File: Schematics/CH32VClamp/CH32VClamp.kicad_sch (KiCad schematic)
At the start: 27 parts, among them J1 USB_C_Receptacle_USB2.0, J2 PGM, J3 OPGM, Q1 SE4625-PandN, Q2 SE4625-PandN, SW2 SW_MEC_5E, U1 ESP32-S2, U2 AP1117-33, Y1 40MHz

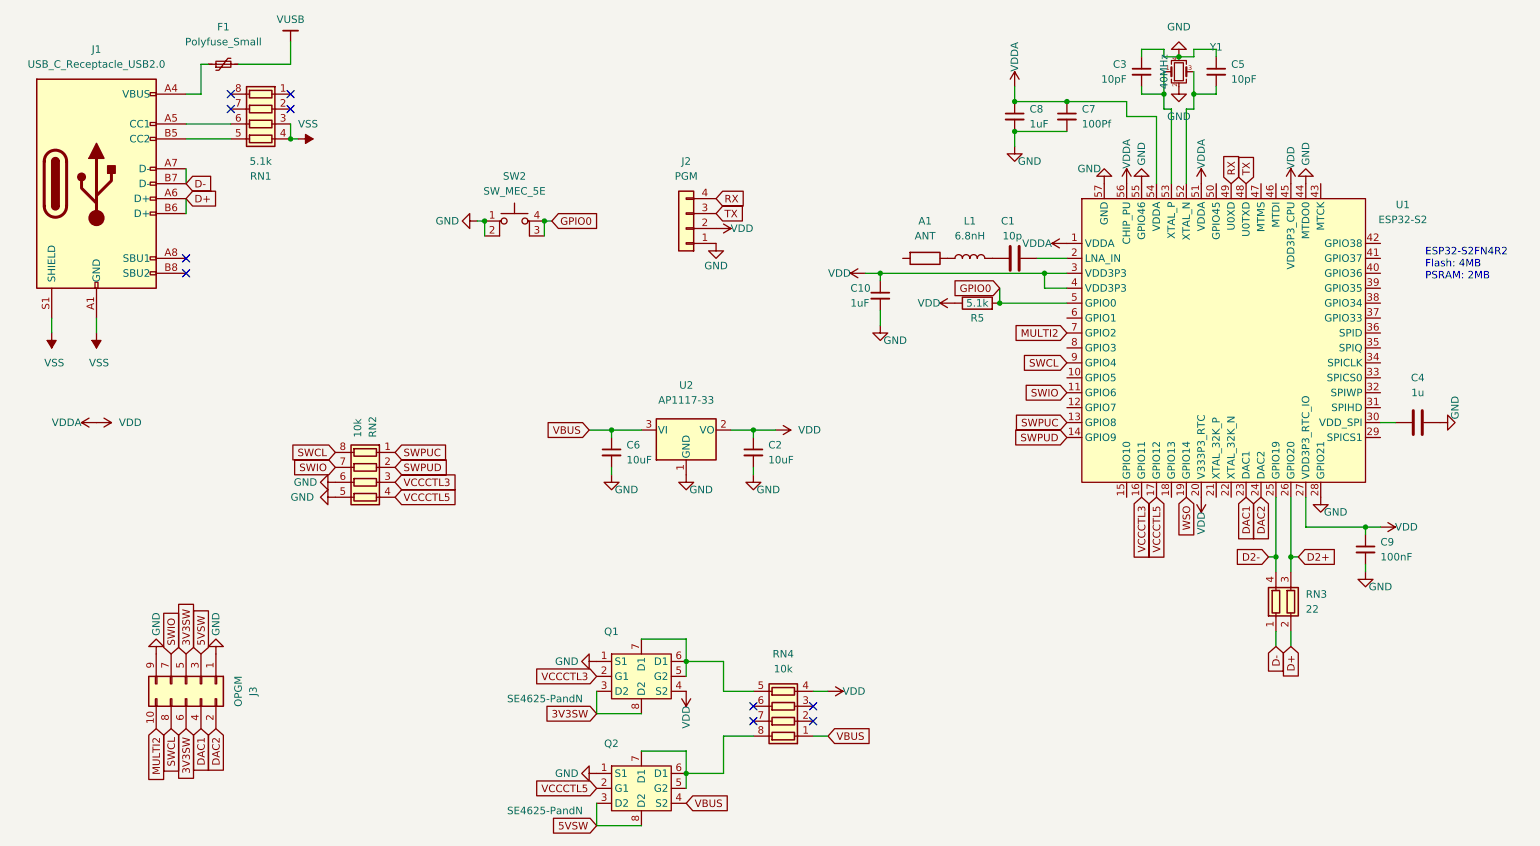
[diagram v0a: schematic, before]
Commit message: Decide on standard and started routing
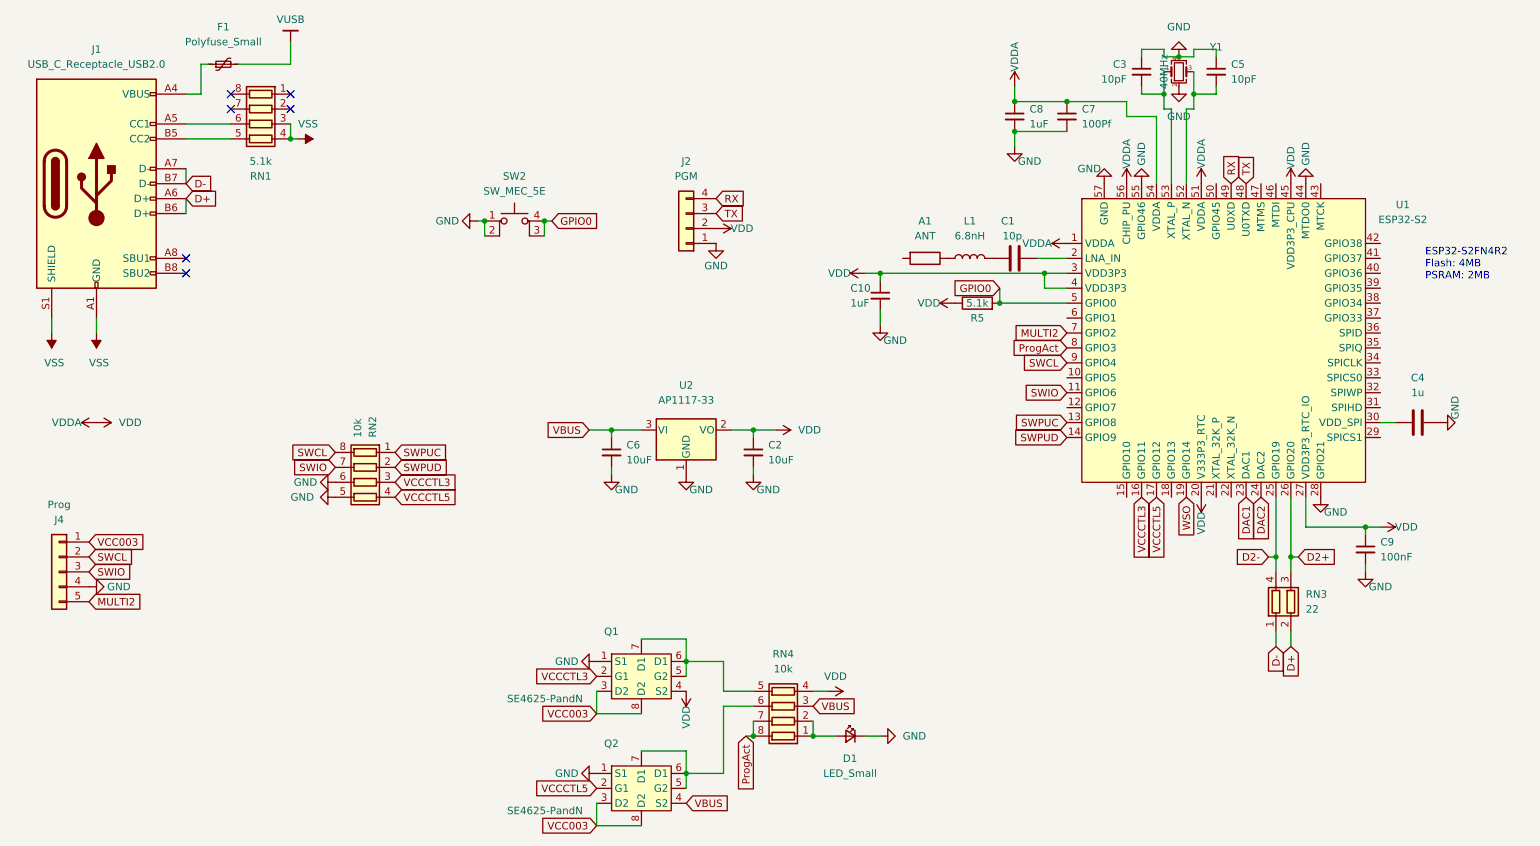
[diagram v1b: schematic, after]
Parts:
- removed J3: OPGM, Connector_PinHeader_2.54mm:PinHeader_2x05_P2.54mm_Horizontal, symbol Connector_Generic:Conn_02x05_Odd_Even
- added D1: LED_Small, LED_SMD:LED_0603_1608Metric, symbol Device:LED_Small
- added J4: Prog, Connector_PinHeader_2.54mm:PinHeader_1x05_P2.54mm_Vertical, symbol Connector_Generic:Conn_01x05
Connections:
- net 5VSW is gone; now on net VCC003: Q2.3 (D2), Q2.8 (D2)
- net GND: now also D1.1 (K), J4.4 (Pin_4)
- net MULTI2: now also J4.5 (Pin_5)
- net SWCL: now also J4.2 (Pin_2)
- net SWIO: now also J4.3 (Pin_3)
- net VBUS: now also RN4.3 (R3.1); no longer RN4.1 (R1.1)
- net ProgAct: now reaches U1.8 (GPIO3)
- net ProgAct: now also RN4.7 (R2.2), RN4.8 (R1.2)
- net at RN4.2 (R2.1): now also RN4.1 (R1.1), D1.2 (A)
- net at RN4.6 (R3.2): now also Q2.5 (G2), Q2.6 (D1), Q2.7 (D1)
- net 3V3SW renamed VCC003
- net VCC003: now also J4.1 (Pin_1)
- no-connect marks 10 -> 6

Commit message: Ordered CH32V Clamp V1
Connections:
- net VSS is gone; now on net GND: J1.A1 (GND), J1.A12 (GND), J1.B1 (GND), J1.B12 (GND), J1.S1 (SHIELD), RN1.3 (R3.1), RN1.4 (R4.1)
- net VUSB is gone; now on net VBUS: F1.2
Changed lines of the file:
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@@
-    (stroke (width 0) (type default))
-  )
-  (wire (pts (xy 66.04 25.4) (xy 66.04 21.59))
     (stroke (width 0) (type default))
   )
@@
     )
   )
+  (global_label "VBUS" (shape input) (at 66.04 25.4 0) (fields_autoplaced)
+    (effects (font (size 1.27 1.27)) (justify left))
+    (property "Intersheetrefs" "${INTERSHEET_REFS}" (at 73.3517 25.4794 0)
+      (effects (font (size 1.27 1.27)) (justify left) hide)
+    )
+  )
   (global_label "VBUS" (shape input) (at 154.94 134.62 0) (fields_autoplaced)
     (effects (font (size 1.27 1.27)) (justify left))
@@
     )
   )
+  (symbol (lib_id "power:GND") (at 33.02 71.12 0) (unit 1)
+    (in_bom yes) (on_board yes) (dnp no)
+    (property "Reference" "#PWR02" (at 33.02 77.47 0)
+      (effects (font (size 1.27 1.27)) hide)
+    )
+    (property "Value" "GND" (at 33.02 76.2 90)
+      (effects (font (size 1.27 1.27)))
+    )
+    (property "Footprint" "" (at 33.02 71.12 0)
+      (effects (font (size 1.27 1.27)) hide)
+    )
+    (property "Datasheet" "" (at 33.02 71.12 0)
+      (effects (font (size 1.27 1.27)) hide)
+    )
+    (pin "1")
+    (instances
+      (project "CH32VClamp"
+        (path "/3c272da4-3810-4d6a-a6aa-4e1cad4b6a87"
+          (reference "#PWR02") (unit 1)
+        )
+      )
+      (project "esp32s2-funprog"
+        (path "/e63e39d7-6ac0-4ffd-8aa3-1841a4541b55"
+          (reference "#PWR0108") (unit 1)
+        )
+      )
+    )
+  )
   (symbol (lib_id "power:VDD") (at 138.43 53.34 270) (unit 1)
     (in_bom yes) (on_board yes) (dnp no)
@@
         (path "/e63e39d7-6ac0-4ffd-8aa3-1841a4541b55"
           (reference "#PWR0119") (unit 1)
+        )
+      )
+    )
+  )
+  (symbol (lib_id "power:GND") (at 25.4 71.12 0) (unit 1)
+    (in_bom yes) (on_board yes) (dnp no)
+    (property "Reference" "#PWR01" (at 25.4 77.47 0)
+      (effects (font (size 1.27 1.27)) hide)
+    )
+    (property "Value" "GND" (at 25.4 76.2 90)
+      (effects (font (size 1.27 1.27)))
+    )
+    (property "Footprint" "" (at 25.4 71.12 0)
+      (effects (font (size 1.27 1.27)) hide)
+    )
+    (property "Datasheet" "" (at 25.4 71.12 0)
+      (effects (font (size 1.27 1.27)) hide)
+    )
+    (pin "1")
+    (instances
+      (project "CH32VClamp"
+        (path "/3c272da4-3810-4d6a-a6aa-4e1cad4b6a87"
+          (reference "#PWR01") (unit 1)
+        )
+      )
+      (project "esp32s2-funprog"
+        (path "/e63e39d7-6ac0-4ffd-8aa3-1841a4541b55"
+          (reference "#PWR0108") (unit 1)
         )
       )
@@
         (path "/e63e39d7-6ac0-4ffd-8aa3-1841a4541b55"
           (reference "#PWR0117") (unit 1)
-        )
-      )
-    )
-  )
-  (symbol (lib_id "power:VSS") (at 33.02 71.12 180) (unit 1)
-    (in_bom yes) (on_board yes) (dnp no)
-    (property "Reference" "#PWR02" (at 33.02 67.31 0)
-      (effects (font (size 1.27 1.27)) hide)
-    )
-    (property "Value" "VSS" (at 31.75 76.2 0)
-      (effects (font (size 1.27 1.27)) (justify right))
-    )
-    (property "Footprint" "" (at 33.02 71.12 0)
-      (effects (font (size 1.27 1.27)) hide)
-    )
-    (property "Datasheet" "" (at 33.02 71.12 0)
-      (effects (font (size 1.27 1.27)) hide)
-    )
-    (pin "1")
-    (instances
-      (project "CH32VClamp"
-        (path "/3c272da4-3810-4d6a-a6aa-4e1cad4b6a87"
-          (reference "#PWR02") (unit 1)
-        )
-      )
-      (project "ReflowReview"
-        (path "/91523ecc-b630-476b-a03e-91f84cd87a20"
-          (reference "#PWR021") (unit 1)
-        )
-      )
-      (project "SerialClamp"
-        (path "/ad13f272-13a7-4209-a78a-add31e33c82c"
-          (reference "#PWR03") (unit 1)
-        )
-      )
-      (project "AccelAssemblyTester"
-        (path "/b10930b8-2990-46a8-9d87-f0faa73d38e1"
-          (reference "#PWR018") (unit 1)
         )
       )
@@
     )
   )
-  (symbol (lib_id "power:VSS") (at 25.4 71.12 180) (unit 1)
-    (in_bom yes) (on_board yes) (dnp no)
-    (property "Reference" "#PWR01" (at 25.4 67.31 0)
-      (effects (font (size 1.27 1.27)) hide)
-    )
-    (property "Value" "VSS" (at 24.13 76.2 0)
-      (effects (font (size 1.27 1.27)) (justify right))
-    )
-    (property "Footprint" "" (at 25.4 71.12 0)
-      (effects (font (size 1.27 1.27)) hide)
-    )
-    (property "Datasheet" "" (at 25.4 71.12 0)
-      (effects (font (size 1.27 1.27)) hide)
-    )
-    (pin "1")
-    (instances
-      (project "CH32VClamp"
-        (path "/3c272da4-3810-4d6a-a6aa-4e1cad4b6a87"
-          (reference "#PWR01") (unit 1)
-        )
-      )
-      (project "ReflowReview"
-        (path "/91523ecc-b630-476b-a03e-91f84cd87a20"
-          (reference "#PWR01") (unit 1)
-        )
-      )
-      (project "SerialClamp"
-        (path "/ad13f272-13a7-4209-a78a-add31e33c82c"
-          (reference "#PWR02") (unit 1)
-        )
-      )
-      (project "AccelAssemblyTester"
-        (path "/b10930b8-2990-46a8-9d87-f0faa73d38e1"
-          (reference "#PWR018") (unit 1)
+  (symbol (lib_id "power:GND") (at 67.31 38.1 90) (unit 1)
+    (in_bom yes) (on_board yes) (dnp no)
+    (property "Reference" "#PWR04" (at 73.66 38.1 0)
+      (effects (font (size 1.27 1.27)) hide)
+    )
+    (property "Value" "GND" (at 72.39 38.1 90)
+      (effects (font (size 1.27 1.27)))
+    )
+    (property "Footprint" "" (at 67.31 38.1 0)
+      (effects (font (size 1.27 1.27)) hide)
+    )
+    (property "Datasheet" "" (at 67.31 38.1 0)
+      (effects (font (size 1.27 1.27)) hide)
+    )
+    (pin "1")
+    (instances
+      (project "CH32VClamp"
+        (path "/3c272da4-3810-4d6a-a6aa-4e1cad4b6a87"
+          (reference "#PWR04") (unit 1)
+        )
+      )
+      (project "esp32s2-funprog"
+        (path "/e63e39d7-6ac0-4ffd-8aa3-1841a4541b55"
+          (reference "#PWR0108") (unit 1)
         )
       )
@@
         (path "/3c272da4-3810-4d6a-a6aa-4e1cad4b6a87"
           (reference "C3") (unit 1)
-        )
-      )
-    )
-  )
-  (symbol (lib_id "power:VSS") (at 67.31 38.1 270) (unit 1)
-    (in_bom yes) (on_board yes) (dnp no)
-    (property "Reference" "#PWR04" (at 63.5 38.1 0)
-      (effects (font (size 1.27 1.27)) hide)
-    )
-    (property "Value" "VSS" (at 67.31 35.56 90)
-      (effects (font (size 1.27 1.27)) (justify left))
-    )
-    (property "Footprint" "" (at 67.31 38.1 0)
-      (effects (font (size 1.27 1.27)) hide)
-    )
-    (property "Datasheet" "" (at 67.31 38.1 0)
-      (effects (font (size 1.27 1.27)) hide)
-    )
-    (pin "1")
-    (instances
-      (project "CH32VClamp"
-        (path "/3c272da4-3810-4d6a-a6aa-4e1cad4b6a87"
-          (reference "#PWR04") (unit 1)
-        )
-      )
-      (project "ReflowReview"
-        (path "/91523ecc-b630-476b-a03e-91f84cd87a20"
-          (reference "#PWR02") (unit 1)
-        )
-      )
-      (project "SerialClamp"
-        (path "/ad13f272-13a7-4209-a78a-add31e33c82c"
-          (reference "#PWR05") (unit 1)
-        )
-      )
-      (project "AccelAssemblyTester"
-        (path "/b10930b8-2990-46a8-9d87-f0faa73d38e1"
-          (reference "#PWR036") (unit 1)
         )
       )
@@
     )
   )
-  (symbol (lib_id "gkl_power:VUSB") (at 66.04 21.59 0) (unit 1)
-    (in_bom yes) (on_board yes) (dnp no) (fields_autoplaced)
-    (property "Reference" "#PWR03" (at 66.04 25.4 0)
-      (effects (font (size 1.27 1.27)) hide)
-    )
-    (property "Value" "VUSB" (at 66.04 17.78 0)
-      (effects (font (size 1.27 1.27)))
-    )
-    (property "Footprint" "" (at 66.04 21.59 0)
-      (effects (font (size 1.27 1.27)) hide)
-    )
-    (property "Datasheet" "" (at 66.04 21.59 0)
-      (effects (font (size 1.27 1.27)) hide)
-    )
-    (pin "1")
-    (instances
-      (project "CH32VClamp"
-        (path "/3c272da4-3810-4d6a-a6aa-4e1cad4b6a87"
-          (reference "#PWR03") (unit 1)
-        )
-      )
-      (project "ReflowReview"
-        (path "/91523ecc-b630-476b-a03e-91f84cd87a20"
-          (reference "#PWR020") (unit 1)
-        )
-      )
-      (project "SerialClamp"
-        (path "/ad13f272-13a7-4209-a78a-add31e33c82c"
-          (reference "#PWR04") (unit 1)
-        )
-      )
-      (project "AccelAssemblyTester"
-        (path "/b10930b8-2990-46a8-9d87-f0faa73d38e1"
-          (reference "#PWR017") (unit 1)
-        )
-      )
-    )
-  )
   (symbol (lib_id "Connector_Generic:Conn_01x05") (at 26.67 111.76 0) (mirror y) (unit 1)
     (in_bom yes) (on_board yes) (dnp no)
@@
       (effects (font (size 1.27 1.27)) hide)
     )
+    (pin "1")
+    (pin "2")
+    (pin "3")
     (pin "4")
     (pin "5")
-    (pin "3")
-    (pin "2")
-    (pin "1")
-    (instances
-      (project "CH32VClamp"
+    (instances
+      (project "CH32VClamp"
